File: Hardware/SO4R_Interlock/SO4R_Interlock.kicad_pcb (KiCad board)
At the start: 4 copper layers, 67.4 x 100.7 mm, 143 parts, among them J1 USB-C 2.0 16P, J2 USB-C 2.0 16P, J3 USB-C 2.0 16P, J4 USB-C 2.0 16P, J5 Header 1x3, J6 RJ45_LED_Shielded, J7 8P8C_LED_Shielded_x4, Q1 2N7002, Q2 2N7002, Q3 2N7002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

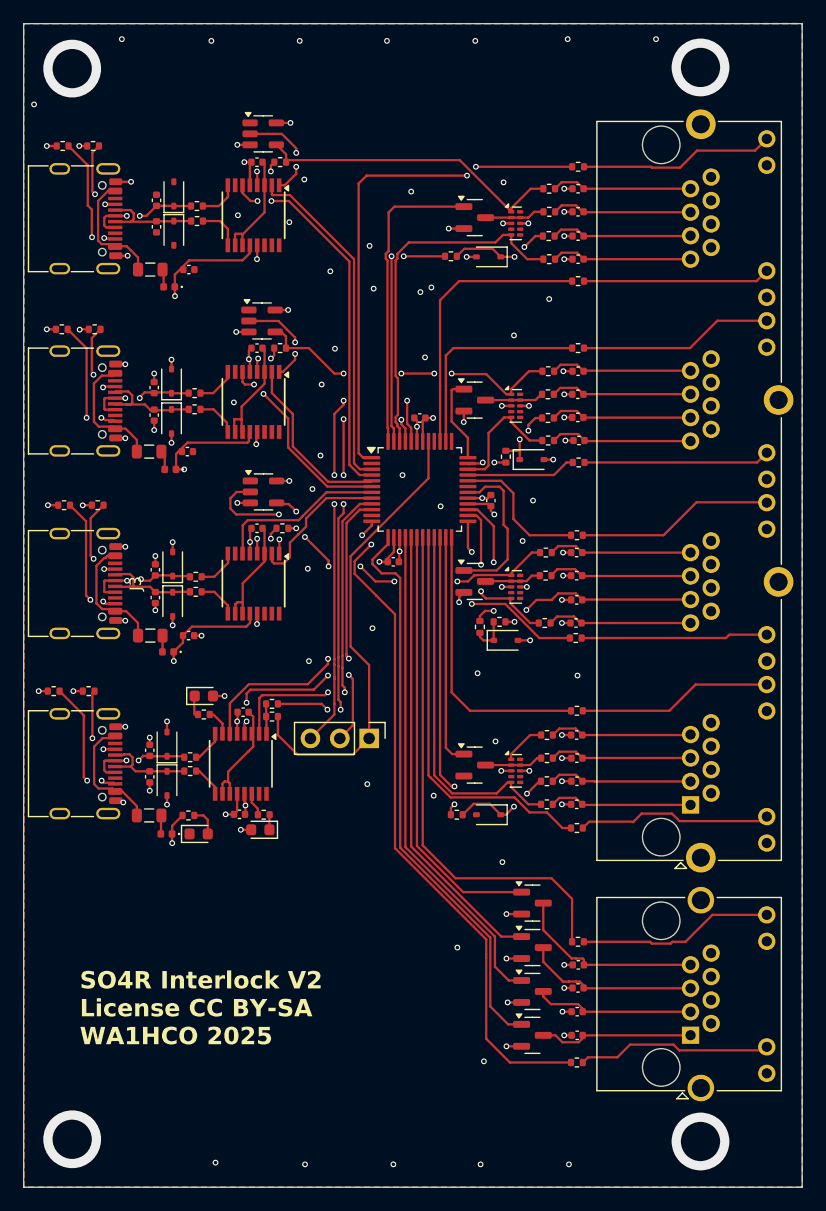
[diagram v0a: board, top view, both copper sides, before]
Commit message: Hardware   better names for PDF in documentation area   started on V2 of hardware   Connected reset\ to VDD on MCU   added .lck to .gitignore Software improves   reading RTS and KEY inputs all at one   writing KEY and PTT output as fast as possible   cleaner concept     Priority derived from RTS and KEY inputs     PTT signals derived from RTS and priority
    Relay signals derived from KEY and priority
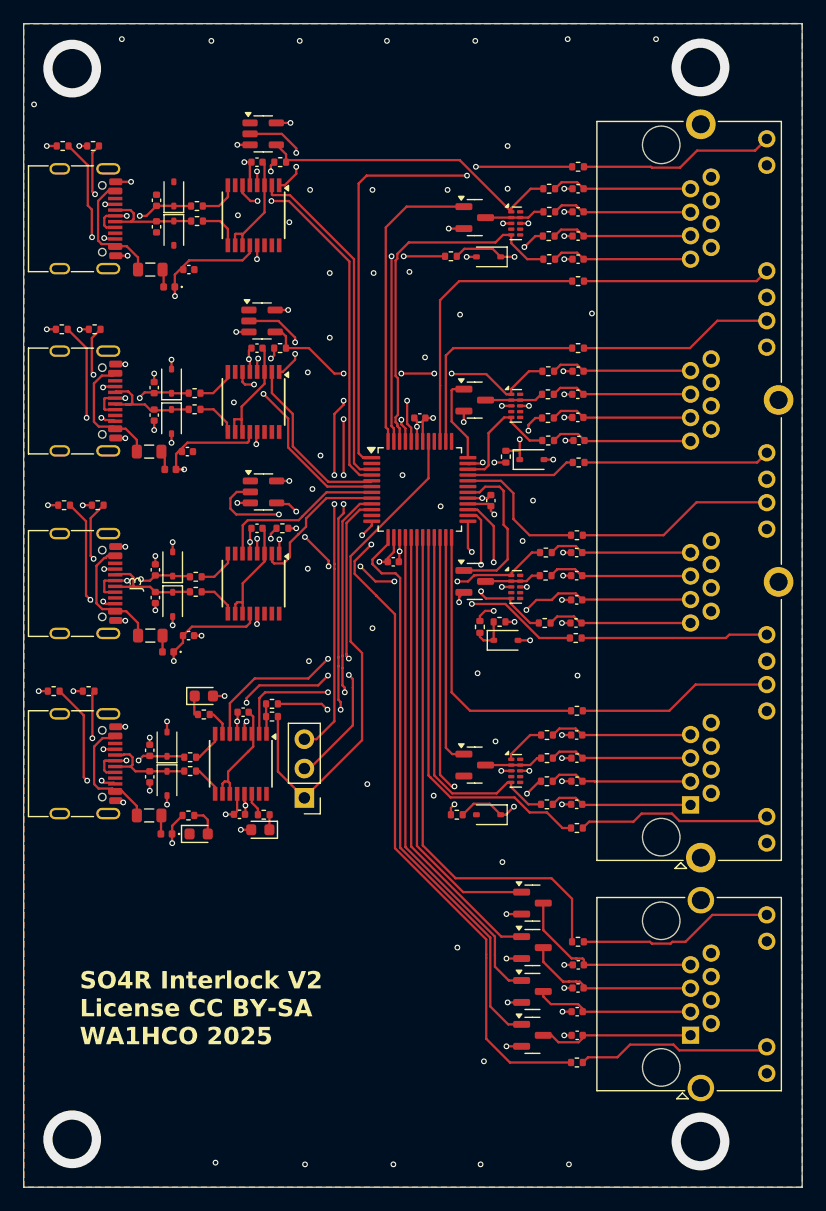
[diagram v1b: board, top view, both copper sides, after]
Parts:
- moved J5 7.62 mm to (127.5, 115.0), turned to 180 degrees
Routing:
- net /UPDI: track 40.0 -> 44.1 mm
- net /RXD1_U: track 19.2 -> 23.1 mm
- net /TXD_M: track 39.7 -> 40.5 mm
- net /PTT4: track 26.7 -> 26.1 mm

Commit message: reversed the RJ45 connectors
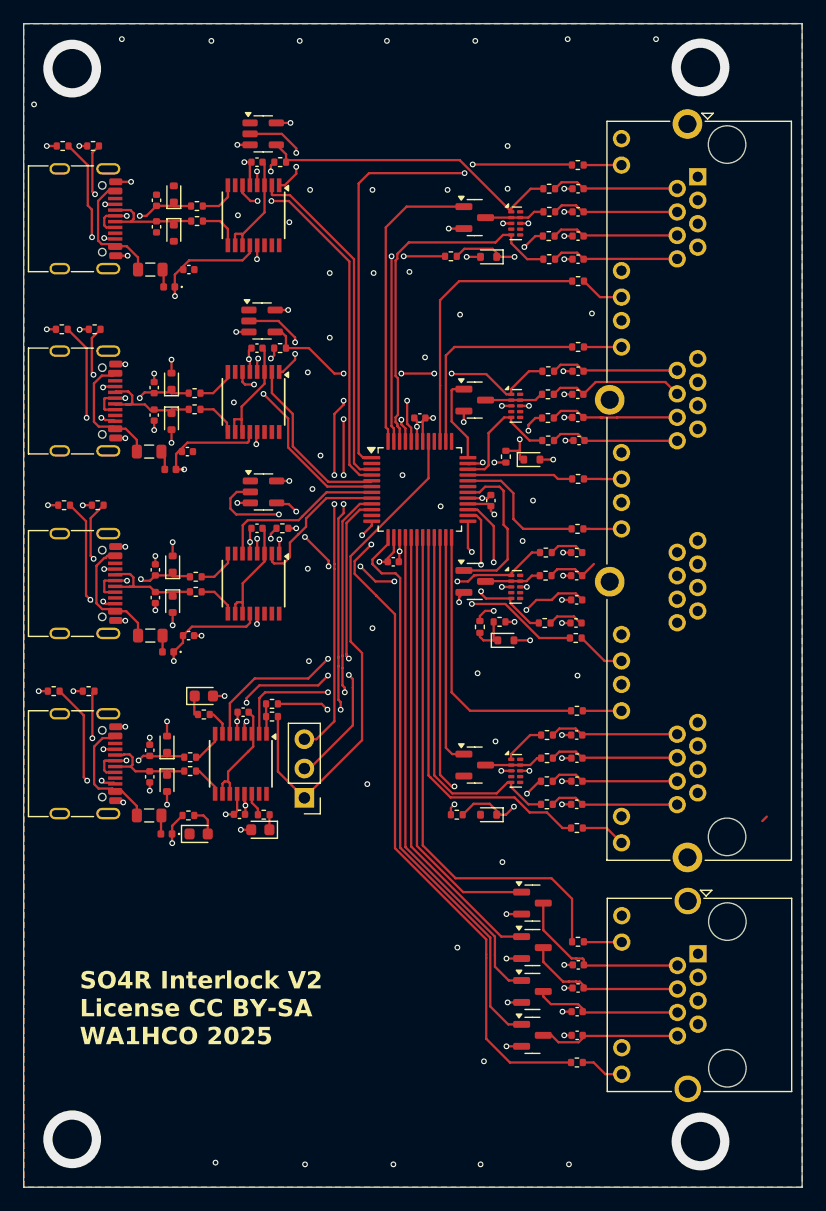
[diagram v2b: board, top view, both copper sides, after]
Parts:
- D1, D10, D11, D12, D16, D17, D18, D19, D2, D3, D4, D9: footprint Diode_SMD:D_SOD-323 -> Diode_SMD:D_SOD-523
- moved J7 54.4 mm to (161.6, 61.3), turned to -90 degrees
- moved J6 7.08 mm to (161.6, 128.5), turned to -90 degrees
- moved R45 1.43 mm to (151.2, 87.4)
- moved R48 0.55 mm to (151.2, 91.8)
- moved R44 0.15 mm to (151.2, 60.2)
- moved R46 0.10 mm to (151.2, 76.0)
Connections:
- J6 pad 1: Net-(Q4-D) -> GND
- J6 pad 2: GND -> Net-(Q1-D)
- J6 pad 3: Net-(Q3-D) -> GND
- J6 pad 4: GND -> Net-(Q2-D)
- J6 pad 5: Net-(Q2-D) -> GND
- J6 pad 6: GND -> Net-(Q3-D)
- J6 pad 7: Net-(Q1-D) -> GND
- J6 pad 8: GND -> Net-(Q4-D)
- J7 pad 1: Net-(C39-Pad2) -> GND
- J7 pad 13: Net-(C38-Pad2) -> GND
- J7 pad 14: GND -> Net-(C25-Pad2)
- J7 pad 15: Net-(C34-Pad2) -> GND
- J7 pad 16: GND -> Net-(C29-Pad2)
- J7 pad 17: Net-(C30-Pad2) -> GND
- J7 pad 18: GND -> Net-(C33-Pad2)
- J7 pad 19: Net-(C26-Pad2) -> GND
- J7 pad 2: GND -> Net-(C24-Pad2)
- J7 pad 20: GND -> Net-(C37-Pad2)
- J7 pad 25: Net-(C37-Pad2) -> GND
- J7 pad 26: GND -> Net-(C26-Pad2)
- J7 pad 27: Net-(C33-Pad2) -> GND
- J7 pad 28: GND -> Net-(C30-Pad2)
- J7 pad 29: Net-(C29-Pad2) -> GND
- J7 pad 3: Net-(C35-Pad2) -> GND
- J7 pad 30: GND -> Net-(C34-Pad2)
- J7 pad 31: Net-(C25-Pad2) -> GND
- J7 pad 32: GND -> Net-(C38-Pad2)
- J7 pad 37: Net-(C36-Pad2) -> GND
- J7 pad 38: GND -> Net-(C27-Pad2)
- J7 pad 39: Net-(C32-Pad2) -> GND
- J7 pad 4: GND -> Net-(C28-Pad2)
- J7 pad 40: GND -> Net-(C31-Pad2)
- J7 pad 41: Net-(C28-Pad2) -> GND
- J7 pad 42: GND -> Net-(C35-Pad2)
- J7 pad 43: Net-(C24-Pad2) -> GND
- J7 pad 44: GND -> Net-(C39-Pad2)
- J7 pad 5: Net-(C31-Pad2) -> GND
- J7 pad 6: GND -> Net-(C32-Pad2)
- J7 pad 7: Net-(C27-Pad2) -> GND
- J7 pad 8: GND -> Net-(C36-Pad2)
- R25 pad 1: Net-(J6-Pad10) -> Net-(J6-Pad12)
- R26 pad 1: Net-(J6-Pad12) -> Net-(J6-Pad10)
- R43 pad 1: Net-(J7-Pad46) -> Net-(J7-Pad12)
- R44 pad 1: Net-(J7-Pad48) -> Net-(J7-Pad10)
- R45 pad 1: Net-(J7-Pad34) -> Net-(J7-Pad24)
- R46 pad 1: Net-(J7-Pad36) -> Net-(J7-Pad22)
- R47 pad 1: Net-(J7-Pad22) -> Net-(J7-Pad36)
- R48 pad 1: Net-(J7-Pad24) -> Net-(J7-Pad34)
- R49 pad 1: Net-(J7-Pad10) -> Net-(J7-Pad48)
- R50 pad 1: Net-(J7-Pad12) -> Net-(J7-Pad46)
- U8 pad 40: /RESET\ -> /5V
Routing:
- net Net-(J7-Pad24): track 17.1 -> 3.25 mm
- net Net-(J6-Pad10): track 16.9 -> 3.30 mm
- net Net-(J7-Pad10): track 16.9 -> 3.28 mm
- net Net-(J6-Pad12): track 16.9 -> 3.79 mm
- net Net-(J7-Pad12): track 16.9 -> 3.82 mm
- net Net-(J7-Pad48): track 16.9 -> 3.88 mm
- net Net-(J7-Pad22): track 16.2 -> 3.25 mm
- net Net-(J7-Pad46): track 16.2 -> 3.35 mm
- net Net-(J7-Pad34): track 16.1 -> 3.30 mm
- net Net-(J7-Pad36): track 16.8 -> 4.27 mm
- net Net-(C38-Pad2): track 12.6 -> 3.18 mm
- net Net-(C26-Pad2): track 12.5 -> 3.14 mm
- net Net-(C34-Pad2): track 17.4 -> 8.13 mm
- net Net-(C30-Pad2): track 12.5 -> 4.62 mm
- net Net-(C35-Pad2): track 12.4 -> 11.2 mm
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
